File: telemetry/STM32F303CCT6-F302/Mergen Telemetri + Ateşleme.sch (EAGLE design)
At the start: 91 parts, among them J2 U.FL, Q2 IRLML6344TRPBF, Q3 IRLML6344TRPBF, U2 BMP280, U3 MPU-6050, U4 L86, U6 AMS1117-3.3, U7 AMS1117-3.3, Y2 ABM3B-26.000MHZ-10-1-U-T

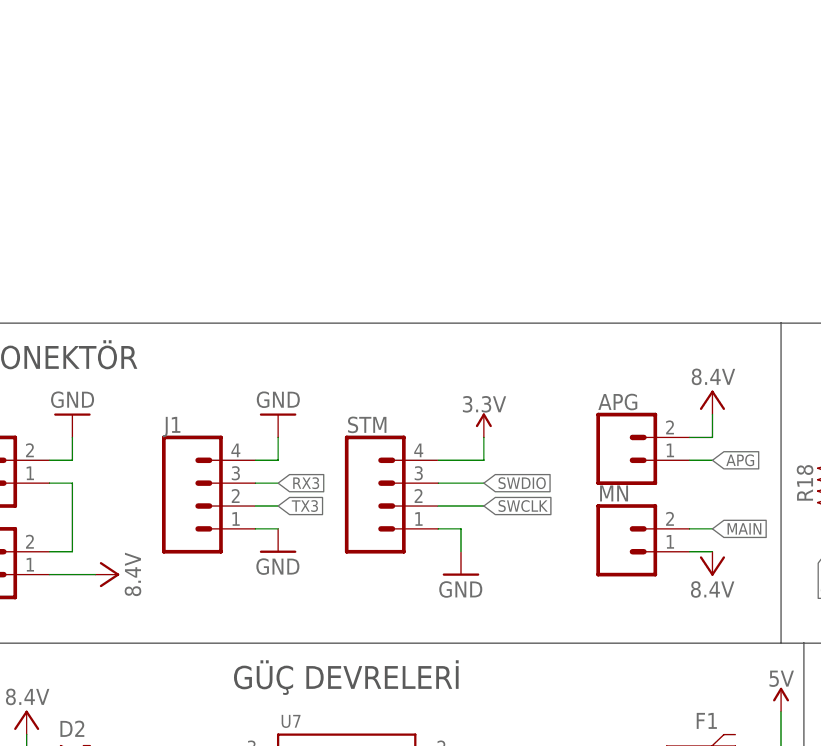
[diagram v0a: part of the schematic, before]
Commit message: Connector was changed and Preparing first order
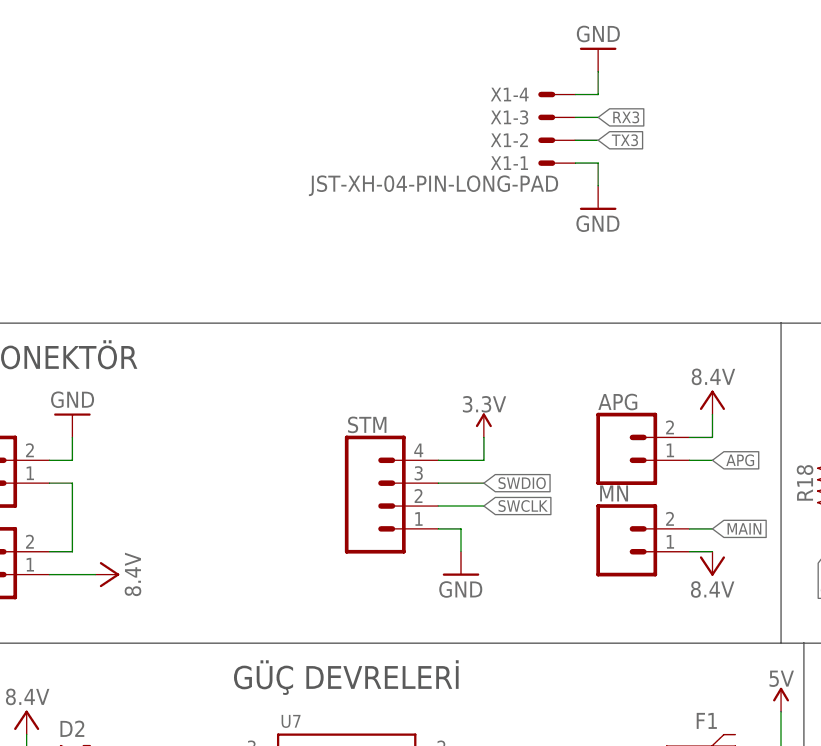
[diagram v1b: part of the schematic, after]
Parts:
- removed J1: (no value), SparkFun-Connectors:CONN_04JST-PTH-VERT
- added X1: JST-XH-04-PIN-LONG-PAD, Rembrandt Electronics - JST XH Connectors v1-0:JST-XH-04-PIN-LONG-PAD
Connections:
- net GND: now also X1-1.S, X1-4.S; no longer J1.1, J1.4
- net RX3: now also X1-3.S; no longer J1.3
- net TX3: now also X1-2.S; no longer J1.2
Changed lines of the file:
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@@
 <part name="ESDA" library="Wurth_EMC Components_WE-TVSP" library_urn="urn:adsk.eagle:library:14283044" deviceset="WE-TVSP_DO-214AC_400W_UNI" device="" package3d_urn="urn:adsk.eagle:package:12146528/2" technology="_824500102" value="12V"/>
 <part name="ESDA1" library="Wurth_EMC Components_WE-TVSP" library_urn="urn:adsk.eagle:library:14283044" deviceset="WE-TVSP_DO-214AC_400W_UNI" device="" package3d_urn="urn:adsk.eagle:package:12146528/2" technology="_824500102" value="12V"/>
-<part name="GND10" library="supply1" library_urn="urn:adsk.eagle:library:371" deviceset="GND" device=""/>
 <part name="SUPPLY17" library="SparkFun-PowerSymbols" library_urn="urn:adsk.eagle:library:530" deviceset="5V" device=""/>
 <part name="C29" library="adafruit" library_urn="urn:adsk.eagle:library:420" deviceset="CPOL-US" device="150CLZ-1010" package3d_urn="urn:adsk.eagle:package:6240454/1" value="1000uF"/>
 <part name="C26" library="adafruit" library_urn="urn:adsk.eagle:library:420" deviceset="CPOL-US" device="150CLZ-1010" package3d_urn="urn:adsk.eagle:package:6240454/1" value="1000uF"/>
 <part name="GND38" library="supply1" library_urn="urn:adsk.eagle:library:371" deviceset="GND" device=""/>
-<part name="J1" library="SparkFun-Connectors" library_urn="urn:adsk.eagle:library:513" deviceset="CONN_04" device="JST-PTH-VERT" package3d_urn="urn:adsk.eagle:package:38102/1"/>
 <part name="D8" library="SparkFun-LED" library_urn="urn:adsk.eagle:library:27167846" deviceset="LED" device="0603" package3d_urn="urn:adsk.eagle:package:27167834/2"/>
 <part name="GND40" library="supply1" library_urn="urn:adsk.eagle:library:371" deviceset="GND" device=""/>
 <part name="GND41" library="supply1" library_urn="urn:adsk.eagle:library:371" deviceset="GND" device=""/>
-<part name="GND2" library="supply1" library_urn="urn:adsk.eagle:library:371" deviceset="GND" device=""/>
 <part name="U1" library="STM32F303" deviceset="STM32F303CCT6" device=""/>
 <part name="SUPPLY13" library="SparkFun-PowerSymbols" deviceset="3.3V" device=""/>
@@
 <part name="R11" library="SparkFun-Resistors" library_urn="urn:adsk.eagle:library:532" deviceset="1KOHM" device="-0603-1/10W-1%" package3d_urn="urn:adsk.eagle:package:39650/1" value="10k"/>
 <part name="SUPPLY21" library="SparkFun-PowerSymbols" library_urn="urn:adsk.eagle:library:530" deviceset="3.3V" device=""/>
+<part name="X1" library="Rembrandt Electronics - JST XH Connectors v1-0" deviceset="JST-XH-04-PIN" device="-LONG-PAD"/>
+<part name="GND21" library="supply1" library_urn="urn:adsk.eagle:library:371" deviceset="GND" device=""/>
+<part name="GND23" library="supply1" library_urn="urn:adsk.eagle:library:371" deviceset="GND" device=""/>
 </parts>
 <sheets>
@@
 <attribute name="VALUE" x="128.27" y="-40.64" size="1.27" layer="96" rot="R90"/>
 </instance>
-<instance part="GND10" gate="1" x="-129.54" y="60.96" smashed="yes">
-<attribute name="VALUE" x="-132.08" y="58.42" size="1.778" layer="96"/>
-</instance>
 <instance part="SUPPLY17" gate="G$1" x="68.58" y="-63.5" smashed="yes">
 <attribute name="VALUE" x="68.58" y="-60.706" size="1.778" layer="96" align="bottom-center"/>
@@
 <attribute name="VALUE" x="66.04" y="-86.36" size="1.778" layer="96"/>
 </instance>
-<instance part="J1" gate="G$1" x="-137.16" y="66.04" smashed="yes">
-<attribute name="VALUE" x="-142.24" y="58.674" size="1.778" layer="96" font="vector"/>
-<attribute name="NAME" x="-142.24" y="74.168" size="1.778" layer="95" font="vector"/>
-</instance>
 <instance part="D8" gate="G$1" x="5.08" y="-76.2" smashed="yes">
 <attribute name="NAME" x="1.651" y="-80.772" size="1.778" layer="95" font="vector" rot="R90"/>
@@
 <attribute name="VALUE" x="35.56" y="-83.82" size="1.778" layer="96"/>
 </instance>
-<instance part="GND2" gate="1" x="-129.54" y="76.2" smashed="yes" rot="R180">
-<attribute name="VALUE" x="-127" y="78.74" size="1.778" layer="96" rot="R180"/>
-</instance>
 <instance part="U1" gate="A" x="7.62" y="45.72" smashed="yes">
 <attribute name="NAME" x="33.3756" y="54.8386" size="2.0828" layer="95" ratio="6" rot="SR0"/>
@@
 <instance part="SUPPLY21" gate="G$1" x="208.28" y="22.86" smashed="yes">
 <attribute name="VALUE" x="208.28" y="25.654" size="1.778" layer="96" align="bottom-center"/>
+</instance>
+<instance part="X1" gate="-1" x="-99.06" y="104.14" smashed="yes" rot="R180">
+<attribute name="NAME" x="-101.6" y="104.902" size="1.524" layer="95" rot="R180"/>
+<attribute name="VALUE" x="-98.298" y="102.743" size="1.778" layer="96" rot="R180"/>
+</instance>
+<instance part="X1" gate="-2" x="-99.06" y="106.68" smashed="yes" rot="R180">
+<attribute name="NAME" x="-101.6" y="107.442" size="1.524" layer="95" rot="R180"/>
+</instance>
+<instance part="X1" gate="-3" x="-99.06" y="109.22" smashed="yes" rot="R180">
+<attribute name="NAME" x="-101.6" y="109.982" size="1.524" layer="95" rot="R180"/>
+</instance>
+<instance part="X1" gate="-4" x="-99.06" y="111.76" smashed="yes" rot="R180">
+<attribute name="NAME" x="-101.6" y="112.522" size="1.524" layer="95" rot="R180"/>
+</instance>
+<instance part="GND21" gate="1" x="-93.98" y="116.84" smashed="yes" rot="R180">
+<attribute name="VALUE" x="-91.44" y="119.38" size="1.778" layer="96" rot="R180"/>
+</instance>
+<instance part="GND23" gate="1" x="-93.98" y="99.06" smashed="yes">
+<attribute name="VALUE" x="-96.52" y="96.52" size="1.778" layer="96"/>
 </instance>
 </instances>
@@
 </segment>
 <segment>
-<pinref part="GND10" gate="1" pin="GND"/>
-<pinref part="J1" gate="G$1" pin="1"/>
-<wire x1="-132.08" y1="63.5" x2="-129.54" y2="63.5" width="0.1524" layer="91"/>
-</segment>
-<segment>
 <pinref part="C29" gate="G$1" pin="-"/>
 <pinref part="GND38" gate="1" pin="GND"/>
@@
 </segment>
 <segment>
-<pinref part="J1" gate="G$1" pin="4"/>
-<wire x1="-132.08" y1="71.12" x2="-129.54" y2="71.12" width="0.1524" layer="91"/>
-<pinref part="GND2" gate="1" pin="GND"/>
-<wire x1="-129.54" y1="71.12" x2="-129.54" y2="73.66" width="0.1524" layer="91"/>
-</segment>
-<segment>
 <pinref part="U1" gate="B" pin="VSSA/VREF-"/>
 <wire x1="5.08" y1="63.5" x2="0" y2="63.5" width="0.1524" layer="91"/>
@@
 <pinref part="C15" gate="G$1" pin="2"/>
 <pinref part="C19" gate="G$1" pin="2"/>
+</segment>
+<segment>
+<pinref part="X1" gate="-4" pin="S"/>
+<wire x1="-96.52" y1="111.76" x2="-93.98" y2="111.76" width="0.1524" layer="91"/>
+<pinref part="GND21" gate="1" pin="GND"/>
+<wire x1="-93.98" y1="111.76" x2="-93.98" y2="114.3" width="0.1524" layer="91"/>
+</segment>
+<segment>
+<pinref part="X1" gate="-1" pin="S"/>
+<wire x1="-96.52" y1="104.14" x2="-93.98" y2="104.14" width="0.1524" layer="91"/>
+<pinref part="GND23" gate="1" pin="GND"/>
+<wire x1="-93.98" y1="104.14" x2="-93.98" y2="101.6" width="0.1524" layer="91"/>
 </segment>
 </net>
@@
 </segment>
 <segment>
-<label x="-129.54" y="66.04" size="1.27" layer="95" xref="yes"/>
-<pinref part="J1" gate="G$1" pin="2"/>
-<wire x1="-132.08" y1="66.04" x2="-129.54" y2="66.04" width="0.1524" layer="91"/>
+<pinref part="X1" gate="-2" pin="S"/>
+<wire x1="-96.52" y1="106.68" x2="-93.98" y2="106.68" width="0.1524" layer="91"/>
+<label x="-93.98" y="106.68" size="1.27" layer="95" xref="yes"/>
 </segment>
 </net>
@@
 </segment>
 <segment>
-<label x="-129.54" y="68.58" size="1.27" layer="95" xref="yes"/>
-<pinref part="J1" gate="G$1" pin="3"/>
-<wire x1="-132.08" y1="68.58" x2="-129.54" y2="68.58" width="0.1524" layer="91"/>
-</segment>
-</net>
+<pinref part="X1" gate="-3" pin="S"/>
+<wire x1="-96.52" y1="109.22" x2="-93.98" y2="109.22" width="0.1524" layer="91"/>
+<label x="-93.98" y="109.22" size="1.27" layer="95" xref="yes"/>
+</segment>
+</net>
